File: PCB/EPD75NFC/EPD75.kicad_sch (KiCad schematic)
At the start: 147 parts, among them J1 Conn_01x26, J10 TF_PUSH, J11 Reset, J12 TC2030-USB-NL-DS, J2 BTN, J3 NFC, J4 BTN, J5 USB-C-Socket-V, J7 USB-C-Socket-V, J8 PWR, Q1 BSS138, U2 ESP32-S3-MINI-1, U2 PN532, U3 MD8942, Y1 27.12MHz

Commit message: New NFC version
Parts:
- added R6: 10K, RevK:R_0603, symbol Device:R
- added SW2: Tamper, RevK:SW_Push_1P1T_NO_6x6mm, symbol Switch:SW_Push
- J2: value BTN -> PWR
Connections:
- net GND: now also SW2.1
- net NFC3V3: now also R6.1
- net at U2.24 (P30/UART_RX): now also R6.2, SW2.2
- no-connect marks 44 -> 43
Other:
- moved on the sheet: C1, C10, C2, C28, C3, C8, C9, D1, D2, D3, D34, D6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

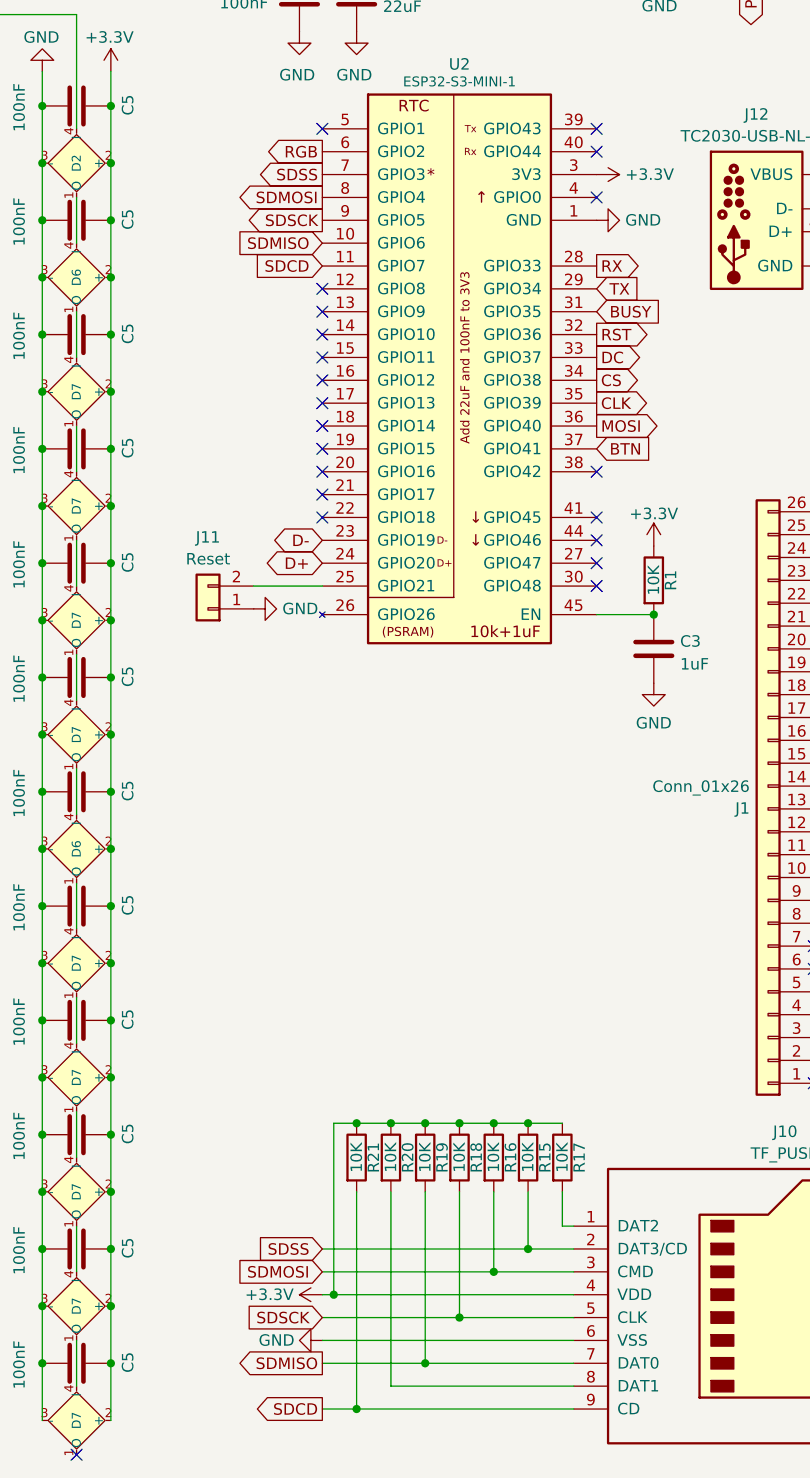
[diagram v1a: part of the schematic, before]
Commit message: New SD card wiring
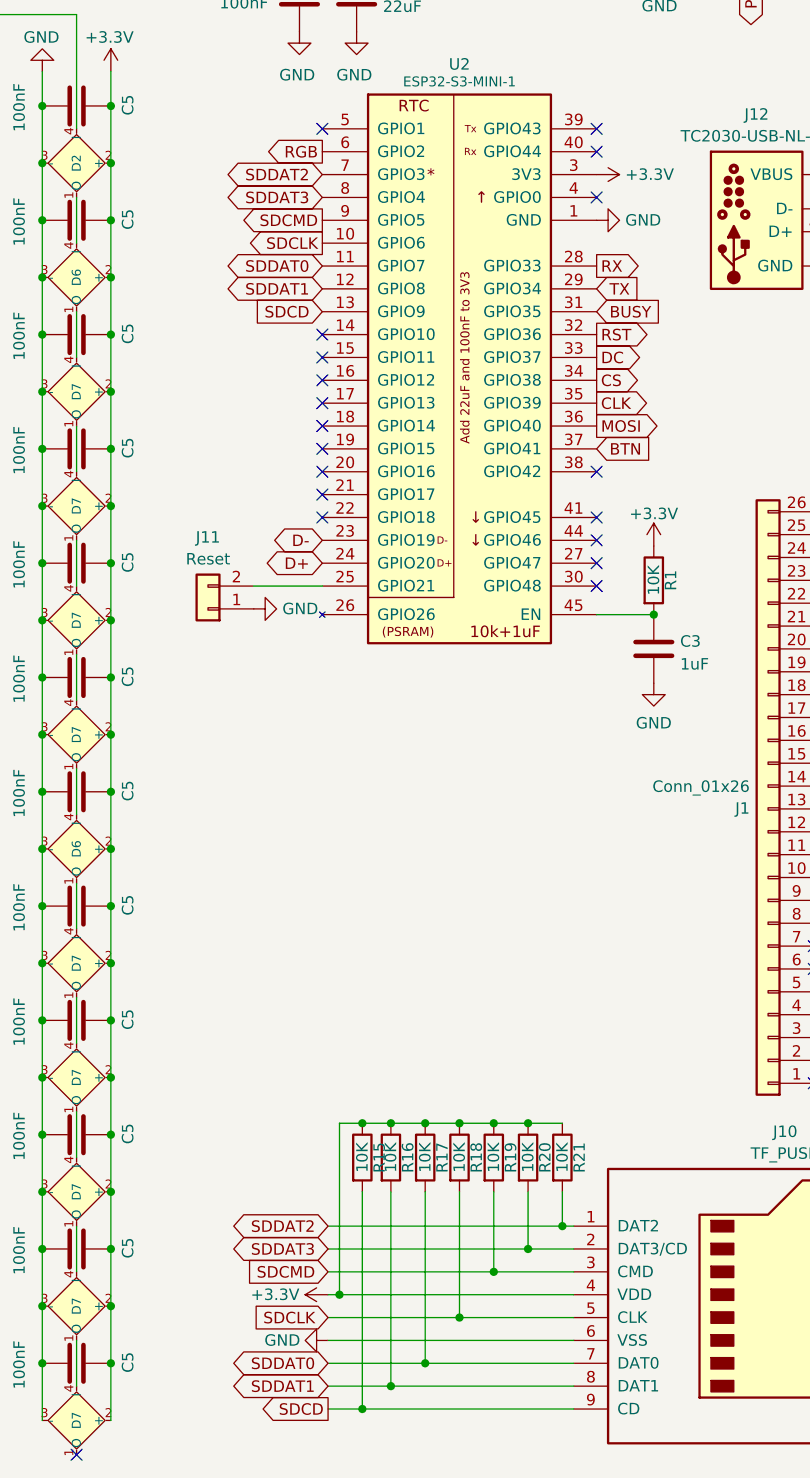
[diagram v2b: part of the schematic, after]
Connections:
- net SDCD: now also R15.2, U2.13 (GPIO9); no longer R21.2, U2.11 (GPIO7)
- net SDDAT0: now reaches R17.2
- net SDDAT0: now also J10.7 (DAT0), U2.11 (GPIO7); no longer J10.1 (DAT2)
- net SDDAT1: now reaches J10.8 (DAT1)
- net SDDAT1: now also R16.2, U2.12 (GPIO8); no longer R20.2
- removed net SDMISO: J10.7 (DAT0), R19.2, U2.10 (GPIO6)
- removed net SDMOSI: J10.3 (CMD), R16.2, U2.8 (GPIO4)
- net SDSCK renamed SDCLK
- net SDCLK: now also U2.10 (GPIO6); no longer U2.9 (GPIO5)
- removed net SDSS: J10.2 (DAT3/CD), R15.2, U2.7 (GPIO3)
- new net SDCMD: J10.3 (CMD), R19.2, U2.9 (GPIO5)
- new net SDDAT2: J10.1 (DAT2), R21.2, U2.7 (GPIO3)
- new net SDDAT3: J10.2 (DAT3/CD), R20.2, U2.8 (GPIO4)
- no-connect marks 43 -> 41

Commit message: PCB Update
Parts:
- C28: JLCPCB Rotation Offset 180 -> (none); LCSC Part # C106188 -> (none); MPN (none) -> C106188
- C8: LCSC Part # C194427 -> (none); MPN (none) -> C194427
- C9: LCSC Part # C1691 -> (none); MPN (none) -> C1691
- D1, D2, D3, D6: LCSC Part # C5204746 -> (none); MPN (none) -> C5204746
- D10, D11, D12, D15, D16, D17, D18, D19, D23, D24, D25, D26, D29, D30, D31, D32, D33, D9: renamed from D7; LCSC Part # C5349953 -> (none); MPN (none) -> C5349953
- D14, D22, D28, D8: renamed from D6; LCSC Part # C5349953 -> (none); MPN (none) -> C5349953
- D21, D35, D5: renamed from D2; LCSC Part # C5349953 -> (none); MPN (none) -> C5349953
- D34, D38, D39: LCSC Part # C5137770 -> (none); MPN (none) -> C5137770
- J1: LCSC Part # C2856831 -> (none); MPN (none) -> C2856831
- J10: LCSC Part # C393941 -> (none); MPN (none) -> C393941
- J2, J4, J8: LCSC Part # C2765055 -> (none); MPN (none) -> C2765055
- J3: LCSC Part # C2765056 -> (none); MPN (none) -> C2765056
- J5, J7: value USB-C-Socket-V -> USB-C-Socket-H; LCSC Part # C709357 -> (none); MPN (none) -> C709357
- L3, L4: LCSC Part # C75639 -> (none); MPN (none) -> C75639
- Q1: JLCPCB Rotation Offset 180 -> (none); LCSC Part # C2938375 -> (none); MPN (none) -> C2938375
- R1: LCSC Part # C2771738 -> (none); MPN (none) -> C2771738
- R25: LCSC Part # C114612 -> (none); MPN (none) -> C114612
- R26: LCSC Part # C22548 -> (none); MPN (none) -> C22548
- R9: LCSC Part # C138062 -> (none); MPN (none) -> C138062
- U2: JLCPCB Rotation Offset -90 -> (none)
- U3: LCSC Part # C2684786 -> (none); MPN (none) -> C2684786
- U4: renamed from U2; LCSC Part # C3013941 -> (none); MPN (none) -> C3013941
- Y1: footprint RevK:Crystal-3.2x2.5 -> (none); JLCPCB Rotation Offset 180 -> (none); LCSC Part # C70591 -> (none); Manufacturer ABRACON -> (none); Part No ABM81-27.120MHZ-10-B1U-T3 -> (none)
- renumbered C3 to C1, C3 to C11, C3 to C12, C3 to C13, C3 to C14, C3 to C15, C3 to C16, C3 to C17, C3 to C18, C28 to C19, C1 to C2, C5 to C20, C8 to C22, C5 to C23, C5 to C24, C5 to C25, C5 to C26, C5 to C27, C5 to C29, C5 to C30, C5 to C31, C5 to C32, C5 to C33, C5 to C34, C5 to C36, C5 to C37, C5 to C38, C5 to C39, C3 to C4, C5 to C40, C5 to C41, C5 to C43, C5 to C44, C5 to C45, C5 to C46, C5 to C47, C5 to C48, C2 to C5, C3 to C6, C3 to C7, R2 to R12, R3 to R13, R1 to R2, R1 to R3, R2 to R4, R3 to R5, R13 to R7, R1 to R8
